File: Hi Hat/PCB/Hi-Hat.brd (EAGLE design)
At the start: 100 x 50 mm, 145 parts, among them IC1 LM741P, IC2 LM741P, IC3 LM741P, IC4 LM741P, IC5 LM741P, IC7 LM741P, IC8 LM741P, Q1 2N3904, Q10 2N2222A, Q11 2N2222A, Q12 2N2222A, Q13 2N2222A, Q14 2N2222A, Q15 2N2222A, Q17 2N3904, Q18 2N3904, Q2 2N3904, Q7 2N2222A, Q8 2N2222A, Q9 2N2222A

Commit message: Created Waveform generator board
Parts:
- removed C51, C52: 0.1uF, resistor:C050-024X044
- removed C53: 22nF, resistor:C050-024X044
- removed C54, C56: 2.2u, resistor:C050-024X044
- removed C55: 1u, resistor:C050-024X044
- removed C57: 10uF, rcl:E2,5-6
- removed C58: 1.5nF, resistor:C050-024X044
- removed C59, C60: 1nF, resistor:C050-024X044
- removed Q18: 2N3904, transistor:TO92
- removed TRIM1, TRIM10, TRIM11, TRIM7, TRIM8, TRIM9: 10k, rcl:RTRIM64W
- added C24, C27: 3.3nF, resistor:C050-024X044
- added C25, C26, C29, C30, C31, C32, C33, C35, C36: 0.1uF, resistor:C050-024X044
- added C28: 22nF, resistor:C050-024X044
- added IC6: LM741P, linear:DIL08
- added Q6: 2N2222A, SparkFun-DiscreteSemi:TO-92
- added R62: 22k, rcl:0207/7
- added R63, R65, R66, R68: 10k, rcl:0207/7
- added R64: 68k, rcl:0207/7
- added R67: 220, rcl:0207/7
- added R69: 47k, rcl:0207/7
- C1, C2, C5, C8, C9: value 0.1uF -> 10uF; device resistor:C050-024X044 -> rcl:E2,5-6
- C13, C14, C15, C16: value 10uF -> 0.1uF; device rcl:E2,5-6 -> resistor:C050-024X044
- C17: value 1u -> 0.1uF
- C18: value 1u -> 47nF
- C19: value 0.1uF -> 47nF
- C20, C21: value 0.1uF -> 33nF
- C22: value 0.1uF -> 0.47uF
- C23: value 0.1uF -> 1nF
- C3: value 10uF -> 1u; device rcl:E2,5-6 -> resistor:C050-024X044
- C4: value 0.1uF -> 1u
- C41: value 47nF -> 1.5nF
- C42: value 47nF -> 1nF
- C43: value 33nF -> 1nF
- C44: value 33nF -> 0.1uF
- C47: value 3.3nF -> 2.2u
- C48: value 3.3nF -> 1u
- C49: value 1nF -> 2.2u
- C50: value 0.47uF -> 10uF; device resistor:C050-024X044 -> rcl:E2,5-6
- Q1, Q2: value 2N3904 -> 2N2222A; device transistor:TO92 -> SparkFun-DiscreteSemi:TO-92
- Q10, Q11, Q12, Q13: value 2N2222A -> (none); device SparkFun-DiscreteSemi:TO-92 -> Capstone:TO-92
- Q14, Q15: value 2N2222A -> 2N3904; device SparkFun-DiscreteSemi:TO-92 -> transistor:TO92
- Q16: value (none) -> 2N3904; device Capstone:TO-92 -> transistor:TO92
- Q3, Q4, Q5: value (none) -> 2N2222A; device Capstone:TO-92 -> SparkFun-DiscreteSemi:TO-92
- R1: value 1k -> 2k
- R12, R17: value 20k -> 10k; device rcl:0207/7 -> rcl:RTRIM64W
- R13, R18, R23: value 10k -> 20k
- R14, R29: value 220k -> 10k
- R2: value 220k -> 2k
- R20, R24, R25: value 20k -> 10k
- R22, R54: device rcl:0207/7 -> rcl:RTRIM64W
- R26: value 68k -> 20k
- R27: value 100k -> 10k; device rcl:0207/7 -> rcl:RTRIM64W
- R28: value 100k -> 20k
- R30: value 47k -> 470k
- R31: value 10k -> 27k
- R33: value 10k -> 220k
- R34: value 82k -> 220k
- R35: value 560 -> 220k
- R36: value 300k -> 220k
- R37: value 10k -> 47k
- R39: value 10k -> 22k
- R41: value 10k -> 82k
- R42: value 10k -> 560
- R43: value 2.7k -> 10k
- R44: value 68k -> 10k
- R45: value 22k -> 10k
- R46: value 27k -> 10k
- R47: value 22k -> 10k; device rcl:0207/7 -> rcl:RTRIM64W
- R48: value 470k -> 10k
- R49: value 10k -> 300k
- R5: value 2k -> 1k
- R50: value 220 -> 10k
- R53: value 47k -> 10k
- R57: value 10k -> 470k
- R58, R8: value 10k -> 100k
- R6: value 2k -> 100k
- R60: value 470k -> 2.7k
- R61, R7: value 100k -> 68k
- R9: value 220k -> 100k
- moved D1 1709.4 mm to (334.0, 533.0)
- moved R47 1508.2 mm to (334.0, 526.0)
- moved R59 1356.0 mm to (1.00, 278.0)
- moved R48 1187.0 mm to (1.00, 228.0)
- moved R49 1187.0 mm to (1.00, 214.0)
- moved R53 1143.0 mm to (1.00, 114.0)
- moved C12 1137.3 mm to (23.0, 45.0), turned to 90 degrees
- moved R52 1115.2 mm to (22.0, 100.0)
- moved Q5 1113.4 mm to (-86.0, 0.00)
- moved C21 1109.8 mm to (-104.0, -22.0)
- moved R51 1085.5 mm to (34.0, 84.0)
- moved R50 1071.1 mm to (13.0, 84.0)
- moved R61 1067.6 mm to (332.0, -203.0)
- moved Q4 1052.3 mm to (-104.0, 0.00)
- moved R38 1009.5 mm to (440.0, 90.0)
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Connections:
- removed net CC_INPUT1: C54.2
- removed net N$37: IC5.6, R40.2
- removed net VCA_INPUT1: R54.1, R55.1
- new net CYMBAL_PREFILTER: C41.1, C42.1, IC7.6, R59.2
- new net N$33: IC8.2, R63.1, R64.2
- new net PRE_CC: C47.2, IC8.6, R64.1
- net +12V: now also C1.+, C25.2, C29.2, C3.2, C32.2, C34.2, C37.2, C39.2, C45.2, IC6.7, Q16.1, Q9.1, R1.2, R12.3, R14.2, R17.3, R20.2, R22.3, R24.2, R25.2, R27.3, R29.2, R65.2, R67.2; no longer C15.+, C17.2, C20.2, C23.2, C46.2, C52.2, C7.2, C9.2, Q15.1, Q18.1, R13.2, R18.2, R22.2, R23.2, R50.2, R52.2, R6.2, R8.2, TRIM10.3, TRIM7.3, TRIM8.3, TRIM9.3
- net -12V: now also C12.2, C2.-, C26.2, C30.2, C33.2, C35.2, C38.2, C4.1, C40.2, C46.2, IC6.4, R2.2, R47.2, R54.2, R62.1, R66.1, R68.1; no longer C10.2, C16.-, C18.1, C19.2, C22.2, C4.2, C45.2, C51.2, C8.2, R45.1, R49.1, R5.2, R51.1, TRIM1.2, TRIM11.2
- net AGND: now also C1.-, C12.1, C2.+, C25.1, C26.1, C29.1, C3.1, C30.1, C32.1, C33.1, C34.1, C35.1, C37.1, C38.1, C39.1, C4.2, C40.1, C41.2, C48.2, C50.-, IC6.3, IC7.3, IC8.3, Q1.3, Q10.2, Q12.2, Q2.3, Q6.3, R30.1, R32.1, R38.1, R40.1, R42.1, R45.1, R52.1, R61.1, R69.1, R9.2; no longer C10.1, C15.-, C16.+, C17.1, C18.2, C19.1, C20.1, C23.1, C4.1, C50.1, C51.1, C52.1, C55.2, C57.-, C58.2, C7.1, C8.1, C9.1, IC3.3, IC5.3, Q14.3, Q16.3, Q4.2, Q5.2, Q9.3, R28.2, R31.1, R33.1, R35.1, R41.1, R44.1, R47.1, R48.1, R53.1, R57.1
- net BRIDGED_T_OUT: now also C28.1, R50.1, R51.1; no longer C53.1
- net CYMBAL_SIGNAL: now also D4.C, D5.A, R57.1; no longer D1.C, D2.A, R60.1
- net FILTER_OUT: now also C44.2, R63.2; no longer C2.2
- net N$1: now also C22.2, D1.C, R31.2; no longer C50.2, D3.C, R46.2
- net N$10: now also IC7.2, R57.2, R58.2, R59.1; no longer IC5.2, R40.1, R60.2, R61.2
- net N$11: now also C14.2, Q1.1, R10.1; no longer C37.2, Q8.1, R8.1
- net N$12: now also C14.1, Q2.2; no longer C37.1, Q7.2
- net N$13: now also C15.2, Q1.2, R13.1; no longer C38.2, Q8.2, R12.1
- net N$14: now also C24.2, IC2.2, R41.1; no longer C47.2, IC7.2, R34.1
- net N$15: now also R13.2; no longer TRIM7.2
- net N$16: now also C16.2, Q3.1; no longer C39.2, Q10.1
- net N$17: now also Q14.2, Q15.2; no longer Q1.2, Q2.2
- net N$18: now also C16.1, Q4.2; no longer C39.1, Q9.2
- net N$19: now also C17.2, Q3.2, R18.1; no longer C40.2, Q10.2, R17.1
- net N$2: now also IC5.3, Q12.1, R51.2, R52.2; no longer IC2.3, Q4.1, R55.2, R57.2
- net N$20: now also C7.1, Q14.3; no longer C6.1, Q1.3
- net N$21: now also C5.-, C6.1, C9.-, R2.1, R6.1; no longer C14.-, C3.-, C5.1, R1.1, R7.1
- net N$22: now also R33.2, R34.2, R35.2, R36.2, R37.1; no longer R14.2, R2.2, R29.2, R30.1, R9.2
- net N$23: now also R7.1, R8.2; no longer R26.1, R27.2
- net N$27: now also C36.1, R55.1; no longer C12.1, R59.1
- net N$28: now also C10.1, R7.2; no longer C1.1, R26.2
- net N$29: now also R18.2; no longer TRIM8.2
- net N$3: now also IC5.2, Q13.1, R50.2, R53.1; no longer IC2.2, Q3.1, R54.2, R58.1
- net N$30: now also C8.+, Q15.1; no longer C13.+, Q2.1
- net N$31: now also C18.2, Q5.1, R20.1; no longer C41.2, Q12.1, R18.1
- net N$32: now also R48.2, R49.1; no longer R36.1, R37.2
- net N$34: now also C31.1, R48.1; no longer C21.1, R37.1
- net N$35: now also C18.1, Q6.2, R21.1; no longer C41.1, Q11.2, R20.1
- net N$36: now also C31.2, IC3.6, R46.2; no longer C21.2, IC8.6, R42.2
- net N$38: now also D2.A, D3.C, R49.2; no longer D4.C, D5.A, R36.2
- net N$39: now also D4.A, D5.C, IC6.6; no longer D1.A, D2.C, IC3.6
- net N$4: now also IC5.5, R54.1; no longer IC2.5, TRIM1.1
- net N$44: now also C19.2, Q5.2, R23.1; no longer C42.2, Q12.2, R21.1
- net N$47: now also C24.1, C27.2, R42.2; no longer C47.1, C48.2, R35.2
- net N$5: now also C9.+, Q15.3, R5.2; no longer C14.+, Q2.3, R1.2
- net N$54: now also R22.2, R23.2; no longer R20.2, TRIM9.2
- net N$55: now also C20.2, Q7.1, R25.1; no longer C43.2, Q14.1, R22.1
- net N$56: now also C20.1, Q8.2, R26.1; no longer C43.1, Q13.2, R24.1
- net N$57: now also C21.2, Q7.2, R28.1; no longer C44.2, Q14.2, R25.1
- net N$58: now also C23.2, R37.2, R38.2; no longer C49.2, R30.2, R31.2
- net N$59: now also R26.2, R27.2, R28.2; no longer R24.2, R25.2, TRIM10.2
- net N$6: now also C5.+, C7.2, R1.1; no longer C3.+, C5.2, R6.1
- net N$60: now also C27.1, C28.2, IC2.6, R41.2; no longer C48.1, C53.2, IC7.6, R34.2
- net N$61: now also IC2.3, R39.2, R40.2; no longer IC7.3, R32.2, R33.2
- net N$62: now also C23.1, R39.1; no longer C49.1, R32.1
- net N$63: now also C47.1, R65.1, R66.2; no longer C54.1, R51.2, R52.1
- net N$64: now also D1.A, Q9.3, R30.2; no longer D3.A, Q15.3, R48.2
- net N$65: now also IC3.3, Q10.1, R44.2, R45.2; no longer IC8.3, Q5.1, R39.2, R41.2
- net N$66: now also IC3.2, Q11.1, R43.2, R46.1; no longer IC8.2, Q16.1, R38.2, R42.1
- net N$67: now also IC3.5, R47.1; no longer IC8.5, TRIM11.1
- net N$68: now also IC3.1, R47.3; no longer IC8.1, TRIM11.3
- net N$7: now also IC5.1, R54.3; no longer IC2.1, TRIM1.3
- net N$71: now also C49.1, R68.2; no longer C56.1, R49.2
- net N$72: now also C48.1, C50.+, R67.1; no longer C55.1, C57.+, R50.1
- net N$73: now also C42.2, C43.1, R60.2; no longer C59.2, C60.1, R43.2
- net N$74: now also C43.2, Q16.2, R61.2; no longer C60.2, Q18.2, R44.2
- net N$75: now also C44.1, Q16.3, R60.1, R62.2; no longer C2.1, Q18.3, R43.1, R45.2
- net N$8: now also IC6.2, R55.2; no longer IC3.2, R59.2
- net N$9: now also C13.2, R8.1; no longer C34.2, R27.1
- net OSC1: now also C15.1, Q2.1, R14.1, R33.1; no longer C38.1, Q7.1, R10.1, R2.1
- net OSC2: now also C17.1, Q4.1, R19.1, R34.1; no longer C40.1, Q9.1, R13.1, R9.1
- net OSC3: now also C19.1, Q6.1, R24.1, R35.1; no longer C42.1, Q11.1, R14.1, R19.1
- net OSC4: now also C21.1, Q8.1, R36.1; no longer C44.1, Q13.1, R23.1
- net OUTPUT: now also C49.2, R69.2; no longer C56.2, R53.2
- net SW1: no longer C58.1, C59.1
- net SW4: now also C36.2, IC5.6, R53.2; no longer C12.2, IC2.6, R58.2
- net TRIGGER: now also Q9.2; no longer Q15.2
- net VCA_TRIGGER: now also Q11.2, Q13.2, R31.1, R32.2; no longer Q16.2, Q3.2, R46.1, R47.2
- net WHITE_NOISE: now also C10.2, C8.-, R6.2; no longer C1.2, C13.-, R7.2
- net WHITE_NOISE_AMP: now also C13.1, R43.1, R44.1, R9.1; no longer C34.1, R28.1, R38.1, R39.1
- net WN_SIGNAL: now also D2.C, D3.A, R58.1; no longer D4.A, D5.C, R61.1

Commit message: Worked on hi-hat
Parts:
- removed C36, C37, C38, C39, C40, C44, C45, C46: 0.1uF, resistor:C050-024X044
- removed C41: 1.5nF, resistor:C050-024X044
- removed C42, C43: 1nF, resistor:C050-024X044
- removed C47, C49: 2.2u, resistor:C050-024X044
- removed C48: 1u, resistor:C050-024X044
- removed C50: 10uF, rcl:E2,5-6
- removed IC8: LM741P, linear:DIL08
- removed Q10, Q11, Q12, Q13: (no value), Capstone:TO-92
- removed Q14, Q15, Q16, Q17: 2N3904, transistor:TO92
- removed Q8, Q9: 2N2222A, SparkFun-DiscreteSemi:TO-92
- removed R12, R47, R54: 10k, rcl:RTRIM64W
- removed R19, R38, R40, R43, R44, R45, R46, R48, R50, R51, R52, R53, R55, R59, R63, R65, R66, R68: 10k, rcl:0207/7
- removed R35, R36, R56: 220k, rcl:0207/7
- removed R37, R69: 47k, rcl:0207/7
- removed R39, R62: 22k, rcl:0207/7
- removed R41: 82k, rcl:0207/7
- removed R42: 560, rcl:0207/7
- removed R49: 300k, rcl:0207/7
- removed R57: 470k, rcl:0207/7
- removed R58: 100k, rcl:0207/7
- removed R60: 2.7k, rcl:0207/7
- removed R61, R64: 68k, rcl:0207/7
- removed R67: 220, rcl:0207/7
- added J1: (no value), SparkFun-Connectors:2X3-NS
- added J2: (no value), SparkFun-Connectors:1X02
- added TRIM1, TRIM2: 10k, rcl:RTRIM64W
- C10: value 0.1uF -> 22nF
- C11: value 0.1uF -> 0.47uF
- C12, C13, C35: value 0.1uF -> 10uF; device resistor:C050-024X044 -> rcl:E2,5-6
- C18, C19: value 47nF -> 0.1uF
- C20, C21: value 33nF -> 0.1uF
- C22: value 0.47uF -> 0.1uF
- C23: value 1nF -> 0.1uF
- C24: value 3.3nF -> 0.1uF
- C26: value 0.1uF -> 1.5nF
- C27: value 3.3nF -> 1nF
- C28: value 22nF -> 1nF
- C32, C34: value 0.1uF -> 2.2u
- C33: value 0.1uF -> 1u
- C5: value 10uF -> 1nF; device rcl:E2,5-6 -> resistor:C050-024X044
- C6: value 0.1uF -> 3.3nF
- C8: value 10uF -> 0.1uF; device rcl:E2,5-6 -> resistor:C050-024X044
- C9: value 10uF -> 3.3nF; device rcl:E2,5-6 -> resistor:C050-024X044
- Q2, Q3, Q4, Q5: value 2N2222A -> (none); device SparkFun-DiscreteSemi:TO-92 -> Capstone:TO-92
- Q6, Q7: value 2N2222A -> 2N3904; device SparkFun-DiscreteSemi:TO-92 -> transistor:TO92
- R1: value 2k -> 22k
- R11, R13, R16, R18, R28: value 20k -> 10k
- R14: value 10k -> 220k
- R17: device rcl:RTRIM64W -> rcl:0207/7
- R2: value 2k -> 10k
- R21: value 20k -> 300k
- R22: value 10k -> 470k; device rcl:RTRIM64W -> rcl:0207/7
- R23: value 20k -> 100k
- R25: value 10k -> 2.7k
- R26: value 20k -> 68k
- R27: value 10k -> 22k; device rcl:RTRIM64W -> rcl:0207/7
- R29: value 10k -> 68k
- R3: value 680k -> 82k
- R30: value 470k -> 10k
- R31: value 27k -> 10k
- R32: value 22k -> 220
- R33: value 220k -> 10k
- R34: value 220k -> 47k
- R4: value 4.7k -> 560
- R5: value 1k -> 470k
- R6: value 100k -> 27k
- R7: value 68k -> 22k
- R8, R9: value 100k -> 10k
- moved C25 729.5 mm to (112.0, -65.0)
- moved C24 710.3 mm to (131.0, -65.0)
- moved C26 686.0 mm to (235.0, -51.0)
- moved C27 661.2 mm to (236.0, -45.0)
- moved C23 612.5 mm to (85.0, 7.00), turned to 270 degrees
- moved D2 604.7 mm to (41.0, 28.0), turned to 270 degrees
- moved D1 595.4 mm to (-83.0, 108.0)
- moved C22 594.1 mm to (98.0, 7.00), turned to 90 degrees
- moved D3 590.2 mm to (37.0, 28.0), turned to 270 degrees
- moved C29 582.6 mm to (211.0, -48.0)
- moved C30 572.9 mm to (200.0, -37.0)
- moved C28 556.5 mm to (236.0, -57.0)
- moved IC3 555.7 mm to (47.0, 42.0), turned to 270 degrees
- moved D5 542.6 mm to (81.0, 17.0), turned to 270 degrees
- moved D4 527.8 mm to (77.0, 17.0), turned to 90 degrees
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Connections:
- removed net N$11: C14.2, Q1.1, R10.1
- removed net N$12: C14.1, Q2.2, R11.1
- removed net N$13: C15.2, Q1.2, R13.1
- removed net N$15: R11.2, R12.2, R13.2
- removed net N$16: C16.2, Q3.1, R15.1
- removed net N$17: Q14.2, Q15.2
- removed net N$18: C16.1, Q4.2, R16.1
- removed net N$19: C17.2, Q3.2, R18.1
- removed net N$20: C7.1, Q14.3, R3.1
- removed net N$21: C5.-, C6.1, C9.-, R2.1, R5.1, R6.1
- removed net N$22: R33.2, R34.2, R35.2, R36.2, R37.1
- removed net N$23: IC1.2, R7.1, R8.2
- removed net N$28: C10.1, R7.2
- removed net N$29: R16.2, R17.2, R18.2
- removed net N$30: C8.+, Q15.1, R4.1
- removed net N$31: C18.2, Q5.1, R20.1
- removed net N$35: C18.1, Q6.2, R21.1
- removed net N$44: C19.2, Q5.2, R23.1
- removed net N$5: C9.+, Q15.3, R5.2
- removed net N$54: R21.2, R22.2, R23.2
- removed net N$55: C20.2, Q7.1, R25.1
- removed net N$56: C20.1, Q8.2, R26.1
- removed net N$57: C21.2, Q7.2, R28.1
- removed net N$58: C23.2, R37.2, R38.2
- removed net N$59: R26.2, R27.2, R28.2
- removed net N$6: C5.+, C6.2, C7.2, R1.1, R3.2, R4.2
- removed net N$9: C13.2, IC1.6, R8.1
- removed net OSC1: C15.1, Q2.1, R14.1, R33.1
- removed net OSC2: C17.1, Q4.1, R19.1, R34.1
- removed net OSC3: C19.1, Q6.1, R24.1, R35.1
- removed net OSC4: C21.1, Q8.1, R29.1, R36.1
- removed net POT2B: SV1.7
- removed net SW4: C36.2, IC5.6, R53.2
- removed net WHITE_NOISE: C10.2, C8.-, R6.2
- removed net WHITE_NOISE_AMP: C13.1, R43.1, R44.1, R9.1
- removed net WN_SIGNAL: D2.C, D3.A, R58.1
- new net SQ_BUFFERED: C5.2, J1.2, J1.4, J1.6
- new net WN_BUFFERED: J1.1, J1.3, J1.5, R15.1, R16.1
- net +12V: now also C14.2, C17.2, C19.2, C22.2, C24.2, C30.2, C7.2, Q1.1, Q6.1, R30.2, R32.2; no longer C11.2, C25.2, C29.2, C32.2, C34.2, C37.2, C39.2, C45.2, IC8.7, Q16.1, Q9.1, R1.2, R10.2, R12.3, R14.2, R15.2, R17.3, R19.2, R20.2, R22.3, R24.2, R25.2, R27.3, R29.2, R65.2, R67.2
- net -12V: now also C15.2, C18.2, C20.2, C23.2, C25.2, C31.2, C8.2, R27.1, R31.1, R33.1, TRIM1.2, TRIM2.2; no longer C12.2, C26.2, C30.2, C33.2, C35.2, C38.2, C40.2, C46.2, IC8.4, R2.2, R47.2, R54.2, R62.1, R66.1, R68.1
- net AGND: now also C12.-, C13.-, C14.1, C15.1, C17.1, C18.1, C19.1, C20.1, C23.1, C24.1, C26.2, C31.1, C33.2, C35.-, C7.1, C8.1, IC3.3, IC5.3, Q2.2, Q4.2, R10.1, R17.1, R2.1, R26.1, R34.1, R4.1, R5.1, R7.1, SV1.7; no longer C12.1, C26.1, C29.1, C32.1, C33.1, C34.1, C35.1, C37.1, C38.1, C39.1, C40.1, C41.2, C45.1, C46.1, C48.2, C50.-, IC1.3, IC4.3, IC8.3, Q1.3, Q10.2, Q10.3, Q11.3, Q12.2, Q12.3, Q13.3, Q6.3, Q7.3, Q8.3, R30.1, R32.1, R38.1, R40.1, R42.1, R45.1, R52.1, R61.1, R69.1, R9.2
- net BRIDGED_T_OUT: now also C10.1, R8.1, R9.1; no longer C28.1, R50.1, R51.1
- net CYMBAL_PREFILTER: now also C26.1, C27.1, IC6.6, R24.2; no longer C41.1, C42.1, IC7.6, R59.2
- net CYMBAL_SIGNAL: now also D2.C, D3.A, R22.1; no longer D4.C, D5.A, R57.1
- net FILTER_OUT: now also C29.2, R28.2; no longer C44.2, R63.2
- net N$1: now also C16.2, IC2.6, R11.2; no longer C22.2, D1.C, R31.2
- net N$10: now also IC6.2, R22.2, R23.2, R24.1; no longer IC7.2, R57.2, R58.2, R59.1
- net N$14: now also C6.2, IC1.2, R3.1; no longer C24.2, IC2.2, R41.1
- net N$2: now also IC2.3, Q2.1, R10.2, R9.2; no longer IC5.3, Q12.1, R51.2, R52.2
- net N$27: now also C16.1, R13.1; no longer C36.1, R55.1
- net N$3: now also IC2.2, Q3.1, R11.1, R8.2; no longer IC5.2, Q13.1, R50.2, R53.1
- net N$32: now also IC5.2, R20.2, R21.1; no longer IC4.2, R48.2, R49.1
- net N$33: now also IC7.2, R28.1, R29.2; no longer IC8.2, R63.1, R64.2
- net N$34: now also C21.1, R20.1; no longer C31.1, R48.1
- net N$36: now also C21.2, IC4.6, R18.2; no longer C31.2, IC3.6, R46.2
- net N$38: now also D4.A, D5.C, IC5.6, R21.2; no longer D2.A, D3.C, IC4.6, R49.2
- net N$39: now also D2.A, D3.C, IC3.6, R14.2; no longer D4.A, D5.C, IC6.6, R56.2
- net N$4: now also IC2.5, TRIM1.1; no longer IC5.5, R54.1
- net N$47: now also C6.1, C9.2, R4.2; no longer C24.1, C27.2, R42.2
- net N$60: now also C10.2, C9.1, IC1.6, R3.2; no longer C27.1, C28.2, IC2.6, R41.2
- net N$61: now also IC1.3, R1.2, R2.2; no longer IC2.3, R39.2, R40.2
- net N$62: now also C5.1, R1.1; no longer C23.1, R39.1
- net N$63: now also C32.1, Q7.2, R30.1, R31.2; no longer C47.1, Q17.2, R65.1, R66.2
- net N$64: now also Q1.3, R5.2; no longer Q9.3, R30.2
- net N$65: now also IC4.3, Q4.1, R16.2, R17.2; no longer IC3.3, Q10.1, R44.2, R45.2
- net N$66: now also IC4.2, Q5.1, R15.2, R18.1; no longer IC3.2, Q11.1, R43.2, R46.1
- net N$67: now also IC4.5, TRIM2.1; no longer IC3.5, R47.1
- net N$68: now also IC4.1, TRIM2.3; no longer IC3.1, R47.3
- net N$7: now also IC2.1, TRIM1.3; no longer IC5.1, R54.3
- net N$71: now also C34.1, Q7.3, R33.2; no longer C49.1, Q17.3, R68.2
- net N$72: now also C33.1, C35.+, Q7.1, R32.1; no longer C48.1, C50.+, Q17.1, R67.1
- net N$73: now also C27.2, C28.1, R25.2; no longer C42.2, C43.1, R60.2
- net N$74: now also C28.2, Q6.2, R26.2; no longer C43.2, Q16.2, R61.2
- net N$75: now also C29.1, Q6.3, R25.1, R27.2; no longer C44.1, Q16.3, R60.1, R62.2
- net N$8: now also IC3.2, R13.2, R14.1; no longer IC6.2, R55.2, R56.1
- net OUTPUT: now also C34.2, R34.2; no longer C49.2, R69.2
- net POT1A: now also D4.C, D5.A, J2.1
- net POT1B: now also J2.2, R23.1
- net POT2A: now also C11.2, C12.+, C13.+, D1.C, R6.2
- net PRE_CC: now also C32.2, IC7.6, R29.1; no longer C47.2, IC8.6, R64.1
- net TRIGGER: now also Q1.2; no longer Q9.2
- net VCA_TRIGGER: now also Q3.2, Q5.2, R6.1, R7.2; no longer Q11.2, Q13.2, R31.1, R32.2
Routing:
- net N$6: track 0.73 -> 0.00 mm
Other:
- board text added: "Cymbals March 18, 2019"
- board text removed: "Snare Drum March 4, 2019"

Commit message: Made more progress on hi-hat
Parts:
- removed C35: 10uF, rcl:E2,5-6
- added R35: 47k, rcl:0207/7
- C13: value 10uF -> 0.1uF; device rcl:E2,5-6 -> resistor:C050-024X044
- C25: value 0.1uF -> 1.5nF
- C26: value 1.5nF -> 1nF
- C28: value 1nF -> 0.1uF
- C31: value 0.1uF -> 2.2u
- C32: value 2.2u -> 1u
- C33: value 1u -> 2.2u
- C34: value 2.2u -> 10uF; device resistor:C050-024X044 -> rcl:E2,5-6
- R27: value 22k -> 0
- R28: value 10k -> 22k
- R29: value 68k -> 10k
- R30: value 10k -> 68k
- R32: value 220 -> 10k
- R33: value 10k -> 220
- R34: value 47k -> 10k
- moved C33 321.1 mm to (-13.0, -11.0)
- moved R34 301.5 mm to (26.0, 6.00)
- moved R31 301.1 mm to (26.0, 18.0)
- moved R32 298.9 mm to (26.0, 14.0)
- moved R33 297.4 mm to (26.0, 10.0)
- moved C32 285.6 mm to (16.0, -8.00)
- moved R30 283.4 mm to (47.0, 22.0)
- moved Q7 279.1 mm to (32.0, 23.0), turned to 180 degrees
- moved C34 260.2 mm to (38.0, 20.0), turned to 90 degrees
- moved C27 201.7 mm to (54.0, 42.0), turned to 90 degrees
- moved C28 193.9 mm to (67.0, 38.0), turned to 270 degrees
- moved R27 190.4 mm to (60.0, 42.0)
- moved C26 185.3 mm to (73.0, 39.0)
- moved R25 182.9 mm to (60.0, 34.0), turned to 180 degrees
- moved R26 181.6 mm to (60.0, 38.0)
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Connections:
- new net N$5: Q6.1, R27.2
- net +12V: now also C13.2, C16.2, C18.2, C21.2, C23.2, C29.2, R27.1, R31.2, R33.2; no longer C14.2, C17.2, C19.2, C22.2, C24.2, C30.2, Q6.1, R30.2, R32.2
- net -12V: now also C14.2, C17.2, C19.2, C22.2, C24.2, C30.2, R28.1, R32.1, R34.1; no longer C15.2, C18.2, C20.2, C23.2, C25.2, C31.2, R27.1, R31.1, R33.1
- net AGND: now also C13.1, C16.1, C21.1, C25.2, C29.1, C32.2, C34.-, R35.1; no longer C13.-, C15.1, C20.1, C25.1, C26.2, C31.1, C33.2, C35.-, R34.1
- net CYMBAL_PREFILTER: now also C25.1; no longer C27.1
- net FILTER_OUT: now also C28.2, R29.2; no longer C29.2, R28.2
- net N$1: now also C15.2; no longer C16.2
- net N$27: now also C15.1; no longer C16.1
- net N$33: now also R29.1, R30.2; no longer R28.1, R29.2
- net N$34: now also C20.1; no longer C21.1
- net N$36: now also C20.2; no longer C21.2
- net N$63: now also C31.1, R31.1, R32.2; no longer C32.1, R30.1, R31.2
- net N$71: now also C33.1, R34.2; no longer C34.1, R33.2
- net N$72: now also C32.1, C34.+, R33.1; no longer C33.1, C35.+, R32.1
- net N$73: now also C26.2, C27.1; no longer C27.2, C28.1
- net N$74: now also C27.2; no longer C28.2
- net N$75: now also C28.1, R28.2; no longer C29.1, R27.2
- net OUTPUT: now also C33.2, R35.2; no longer C34.2, R34.2
- net POT2A: no longer C13.+
- net PRE_CC: now also C31.2, R30.1; no longer C32.2, R29.1

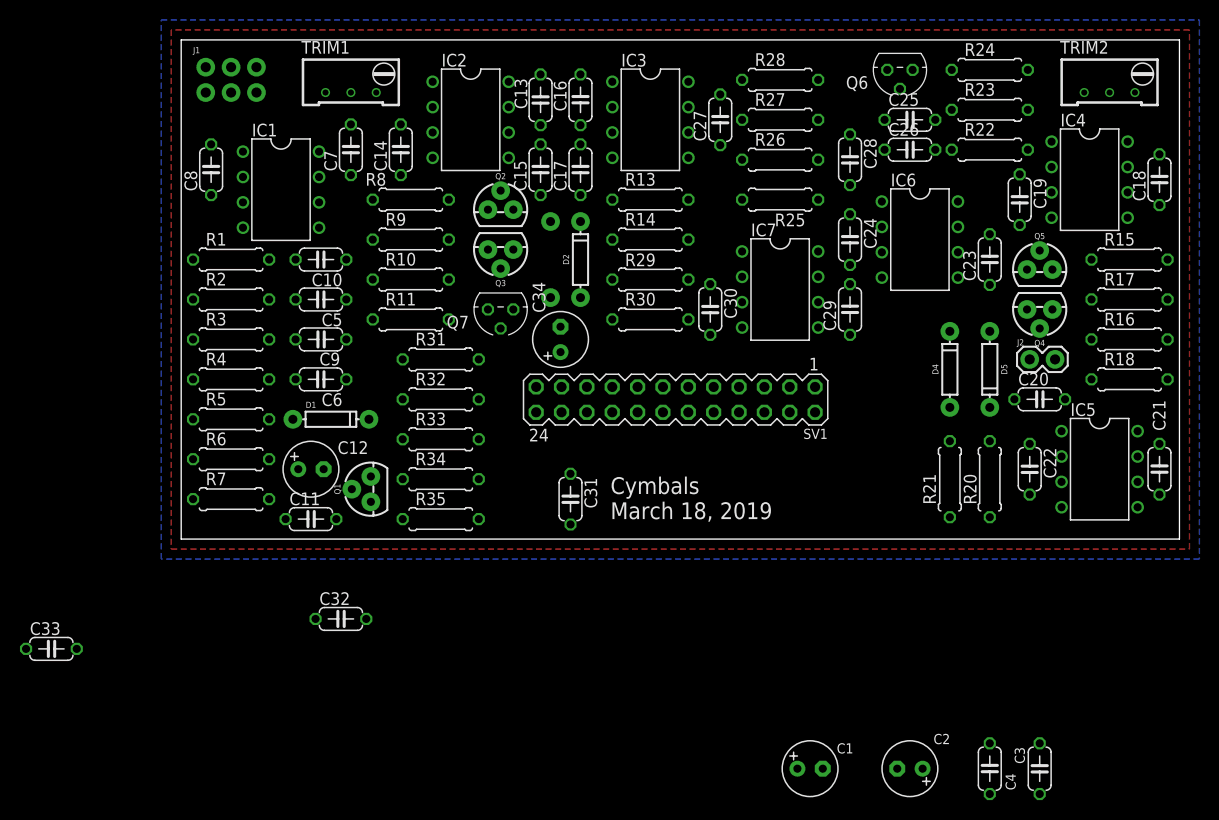
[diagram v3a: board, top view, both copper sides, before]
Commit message: worked more on laying out PCB
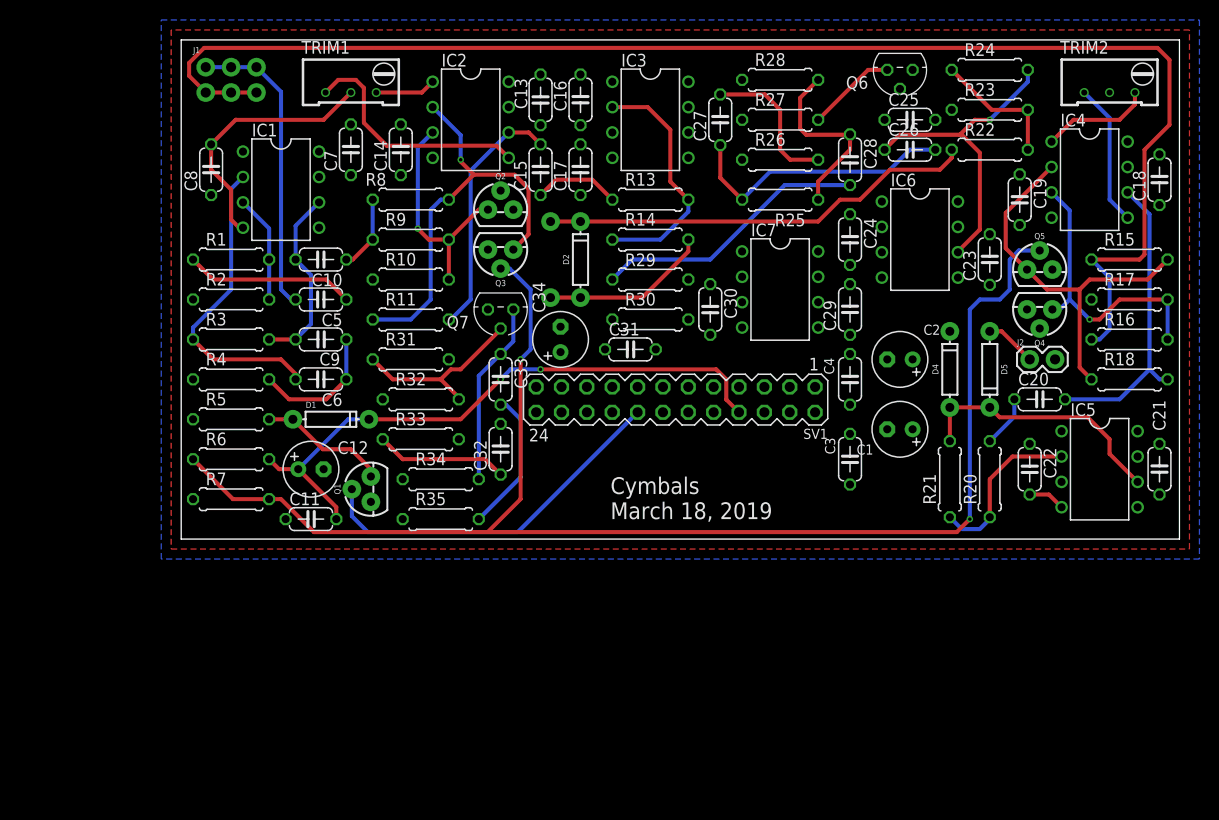
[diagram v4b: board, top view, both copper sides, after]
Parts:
- moved C33 52.5 mm to (32.0, 16.0), turned to 270 degrees
- moved C4 41.4 mm to (67.0, 16.0), turned to 270 degrees
- moved C2 41.0 mm to (72.0, 18.0)
- moved C3 36.4 mm to (67.0, 8.00)
- moved C1 35.2 mm to (72.0, 11.0), turned to 180 degrees
- moved C32 23.3 mm to (32.0, 9.00), turned to 90 degrees
- moved C31 16.2 mm to (45.0, 19.0), turned to 0 degrees
- moved R31 3.00 mm to (23.0, 18.0)
- moved R32 2.00 mm to (24.0, 14.0)
- moved R33 2.00 mm to (24.0, 10.0)
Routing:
- net WN_BUFFERED: track 0.00 -> 144.1 mm
- net VCA_TRIGGER: track 0.00 -> 143.5 mm, vias 0 -> 2
- net POT2A: track 0.00 -> 61.2 mm, vias 0 -> 2
- net CYMBAL_SIGNAL: track 0.00 -> 43.6 mm
- net N$3: track 0.00 -> 42.7 mm, vias 0 -> 1
- net N$66: track 0.00 -> 38.7 mm
- net TRIGGER: track 0.00 -> 37.0 mm
- net CYMBAL_PREFILTER: track 0.00 -> 32.0 mm, vias 0 -> 1
- net N$14: track 0.00 -> 30.6 mm
- net N$36: track 0.00 -> 30.6 mm
- net SQ_BUFFERED: track 0.00 -> 30.2 mm
- net -12V: track 0.00 -> 29.8 mm
- net N$65: track 0.00 -> 29.1 mm, vias 0 -> 1
- net N$73: track 0.00 -> 27.8 mm
- net FILTER_OUT: track 0.00 -> 27.7 mm
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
